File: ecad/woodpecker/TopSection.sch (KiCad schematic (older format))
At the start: 0 parts

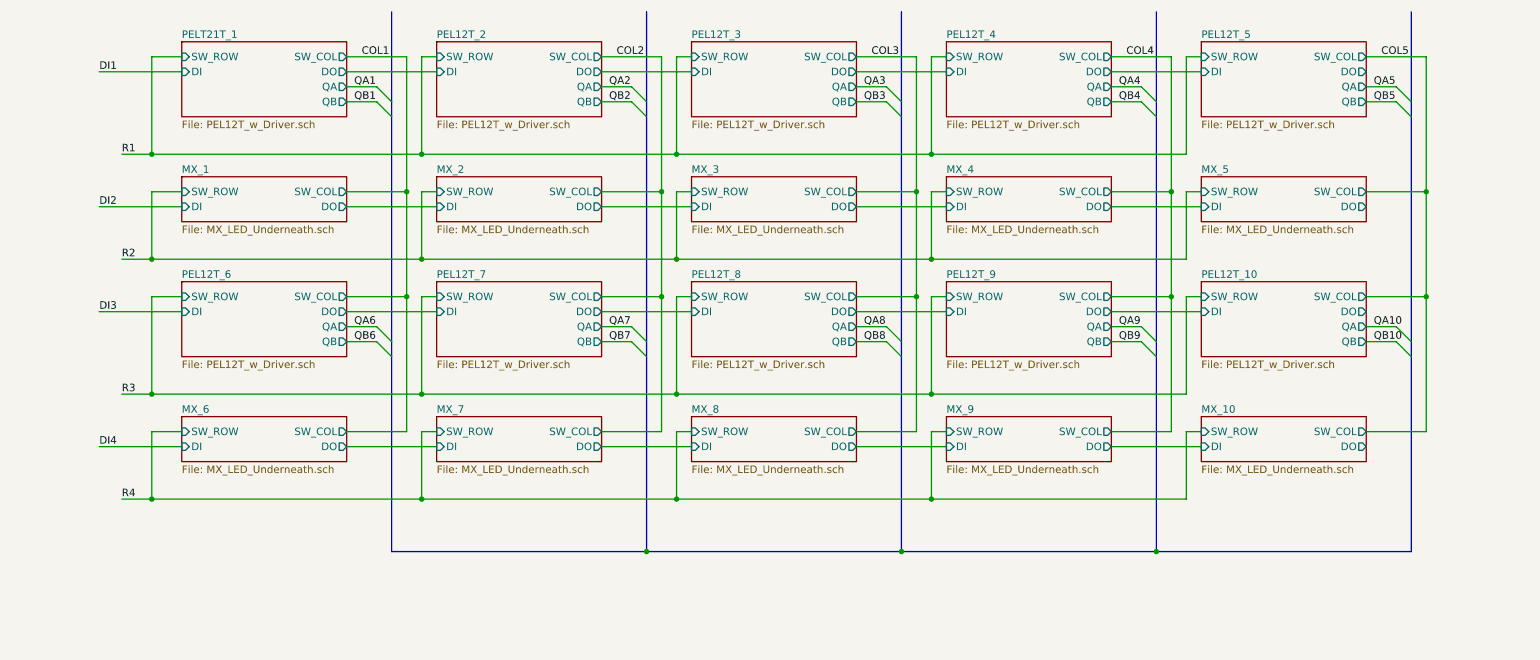
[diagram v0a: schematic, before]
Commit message: Adds bottom section in monolithic design
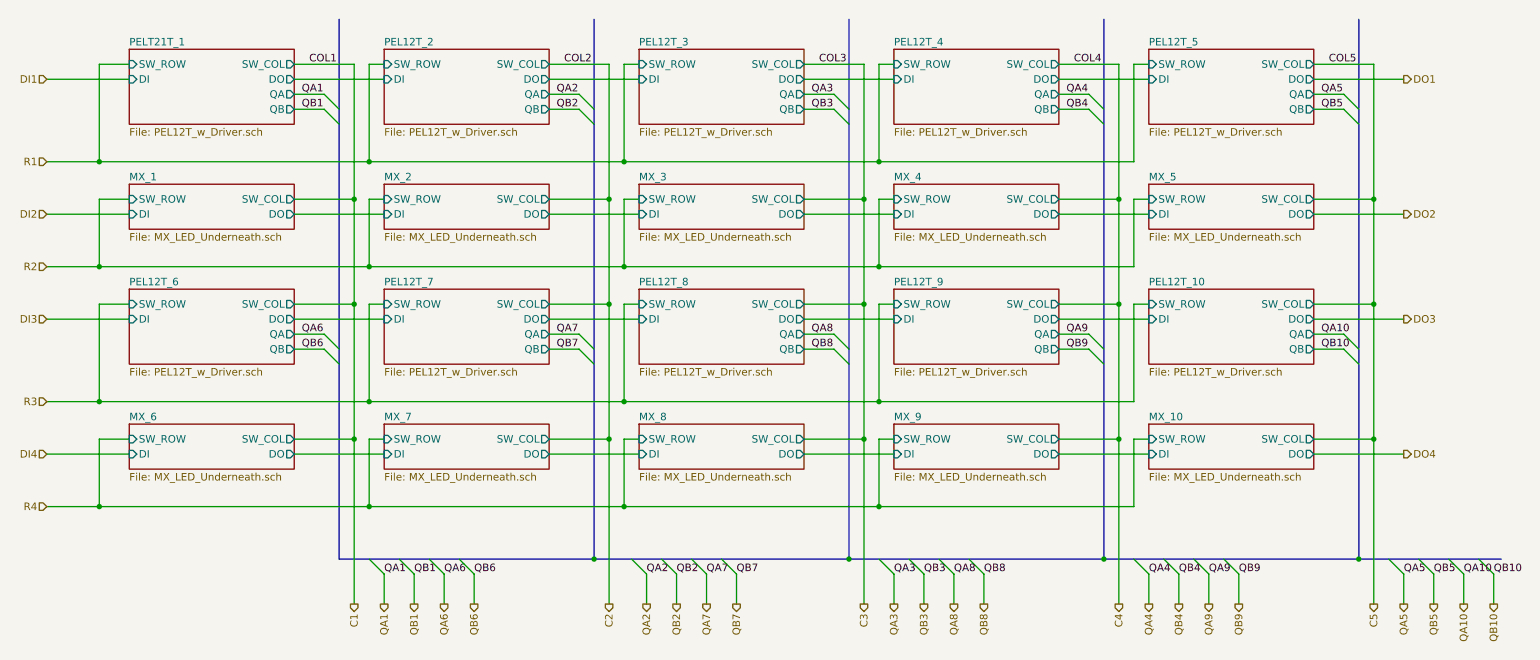
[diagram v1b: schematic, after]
